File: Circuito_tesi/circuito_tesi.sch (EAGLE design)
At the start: 21 parts, among them IC1 317T, IC2 317T, IC3 317T, U1 NRF52832, U2 BME688, X1 OPAMP, X2 OPAMP

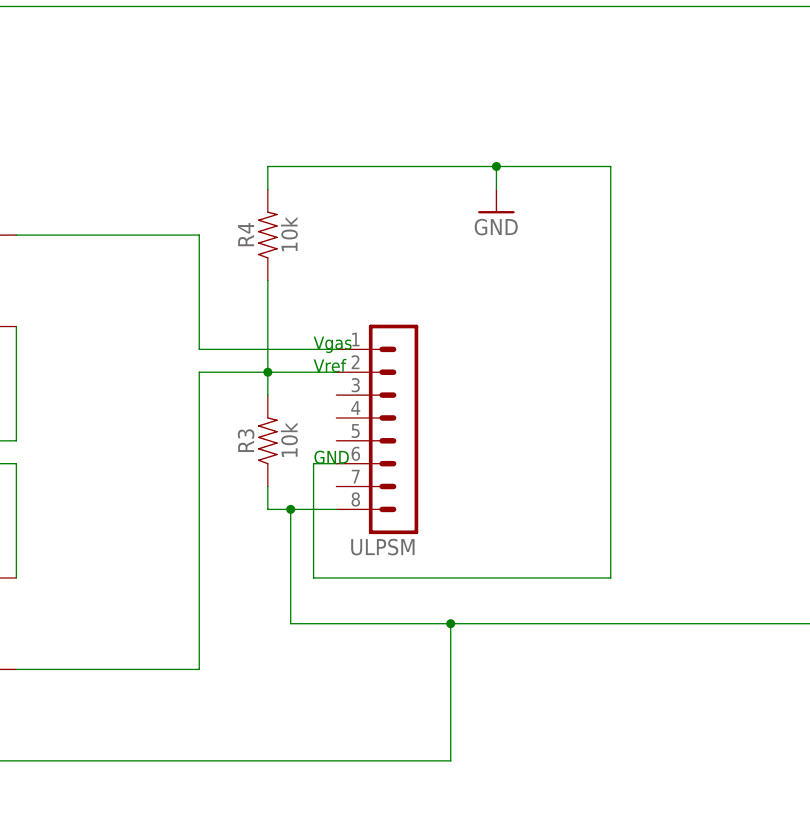
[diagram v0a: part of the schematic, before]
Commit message: Attivato saadc
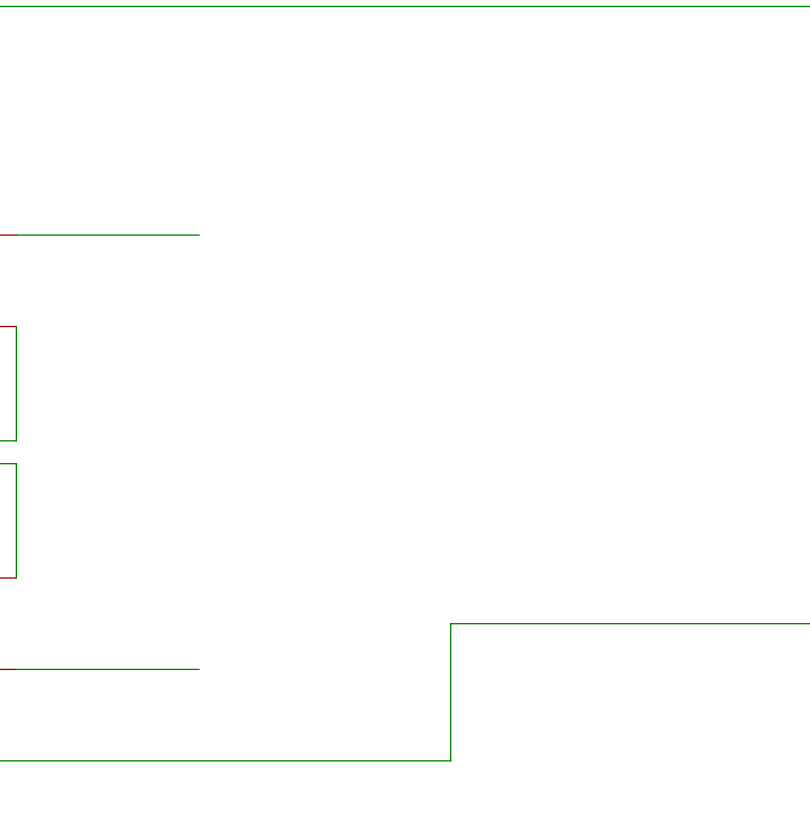
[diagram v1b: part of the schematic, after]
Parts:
- removed R3, R4: 10k, SparkFun-Resistors:10KOHM-HORIZ-1/6W-5%
- removed ULPSM: (no value), con-lstb:MA08-1
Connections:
- net 3.3: no longer R3.1, R4.2, ULPSM.6, ULPSM.8
- net N$10: no longer ULPSM.1
- net N$6: no longer R3.2, R4.1, ULPSM.2
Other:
- note removed: "GND"
- note removed: "Vgas"
- note removed: "Vref"
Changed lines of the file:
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@@
 <part name="R2" library="SparkFun-Resistors" deviceset="10KOHM" device="-HORIZ-1/6W-5%" value="10k"/>
 <part name="GND7" library="supply" deviceset="GND" device=""/>
-<part name="ULPSM" library="con-lstb" library_urn="urn:adsk.eagle:library:162" deviceset="MA08-1" device="" package3d_urn="urn:adsk.eagle:package:8343/1"/>
-<part name="R3" library="SparkFun-Resistors" deviceset="10KOHM" device="-HORIZ-1/6W-5%" value="10k"/>
-<part name="R4" library="SparkFun-Resistors" deviceset="10KOHM" device="-HORIZ-1/6W-5%" value="10k"/>
-<part name="GND8" library="supply" deviceset="GND" device=""/>
 <part name="X1" library="ngspice-simulation" library_urn="urn:adsk.eagle:library:527439" deviceset="OPAMP" device=""/>
 <part name="X2" library="ngspice-simulation" library_urn="urn:adsk.eagle:library:527439" deviceset="OPAMP" device=""/>
@@
 <text x="-132.08" y="104.14" size="1.4224" layer="91">SDA</text>
 <text x="-132.08" y="78.74" size="1.4224" layer="91">SCL</text>
-<text x="48.26" y="185.42" size="1.4224" layer="91">GND</text>
-<text x="48.26" y="198.12" size="1.4224" layer="91">Vgas</text>
-<text x="48.26" y="195.58" size="1.4224" layer="91">Vref</text>
 <text x="-220.98" y="86.36" size="5.08" layer="91">BME688</text>
 </plain>
@@
 <instance part="GND7" gate="1" x="-193.04" y="83.82" smashed="yes">
 <attribute name="VALUE" x="-195.58" y="81.28" size="1.778" layer="96"/>
-</instance>
-<instance part="ULPSM" gate="1" x="58.42" y="190.5" smashed="yes" rot="R180">
-<attribute name="VALUE" x="59.69" y="203.2" size="1.778" layer="96" rot="R180"/>
-<attribute name="NAME" x="59.69" y="177.038" size="1.778" layer="95" rot="R180"/>
-</instance>
-<instance part="R3" gate="G$1" x="43.18" y="187.96" smashed="yes" rot="R90">
-<attribute name="NAME" x="41.656" y="187.96" size="1.778" layer="95" font="vector" rot="R90" align="bottom-center"/>
-<attribute name="VALUE" x="44.704" y="187.96" size="1.778" layer="96" font="vector" rot="R90" align="top-center"/>
-</instance>
-<instance part="R4" gate="G$1" x="43.18" y="210.82" smashed="yes" rot="R90">
-<attribute name="NAME" x="41.656" y="210.82" size="1.778" layer="95" font="vector" rot="R90" align="bottom-center"/>
-<attribute name="VALUE" x="44.704" y="210.82" size="1.778" layer="96" font="vector" rot="R90" align="top-center"/>
-</instance>
-<instance part="GND8" gate="1" x="68.58" y="213.36" smashed="yes">
-<attribute name="VALUE" x="66.04" y="210.82" size="1.778" layer="96"/>
 </instance>
 <instance part="X1" gate="G$1" x="2.54" y="205.74" smashed="yes" rot="MR0">
@@
 </segment>
 <segment>
-<pinref part="R4" gate="G$1" pin="2"/>
-<wire x1="43.18" y1="215.9" x2="43.18" y2="218.44" width="0.1524" layer="91"/>
-<wire x1="43.18" y1="218.44" x2="68.58" y2="218.44" width="0.1524" layer="91"/>
-<pinref part="GND8" gate="1" pin="GND"/>
-<wire x1="68.58" y1="218.44" x2="68.58" y2="215.9" width="0.1524" layer="91"/>
-<pinref part="ULPSM" gate="1" pin="6"/>
-<wire x1="50.8" y1="185.42" x2="48.26" y2="185.42" width="0.1524" layer="91"/>
-<wire x1="48.26" y1="185.42" x2="48.26" y2="172.72" width="0.1524" layer="91"/>
-<wire x1="48.26" y1="172.72" x2="81.28" y2="172.72" width="0.1524" layer="91"/>
-<wire x1="81.28" y1="172.72" x2="81.28" y2="218.44" width="0.1524" layer="91"/>
-<wire x1="81.28" y1="218.44" x2="68.58" y2="218.44" width="0.1524" layer="91"/>
-<junction x="68.58" y="218.44"/>
-</segment>
-<segment>
 <pinref part="X1" gate="G$1" pin="VSS"/>
 <pinref part="GND9" gate="1" pin="GND"/>
@@
 <wire x1="-228.6" y1="104.14" x2="-228.6" y2="119.38" width="0.1524" layer="91"/>
 <wire x1="111.76" y1="71.12" x2="-228.6" y2="71.12" width="0.1524" layer="91"/>
-<pinref part="ULPSM" gate="1" pin="8"/>
-<wire x1="50.8" y1="180.34" x2="45.72" y2="180.34" width="0.1524" layer="91"/>
-<wire x1="45.72" y1="180.34" x2="45.72" y2="167.64" width="0.1524" layer="91"/>
-<wire x1="45.72" y1="167.64" x2="63.5" y2="167.64" width="0.1524" layer="91"/>
 <junction x="111.76" y="167.64"/>
 <wire x1="63.5" y1="167.64" x2="111.76" y2="167.64" width="0.1524" layer="91"/>
-<wire x1="45.72" y1="180.34" x2="43.18" y2="180.34" width="0.1524" layer="91"/>
-<junction x="45.72" y="180.34"/>
-<pinref part="R3" gate="G$1" pin="1"/>
-<wire x1="43.18" y1="180.34" x2="43.18" y2="182.88" width="0.1524" layer="91"/>
 <pinref part="B1" gate="G$1" pin="LV"/>
 <pinref part="IC2" gate="A1" pin="VO"/>
@@
 <wire x1="0" y1="152.4" x2="63.5" y2="152.4" width="0.1524" layer="91"/>
 <wire x1="63.5" y1="152.4" x2="63.5" y2="167.64" width="0.1524" layer="91"/>
-<junction x="63.5" y="167.64"/>
 <wire x1="-228.6" y1="119.38" x2="-190.5" y2="119.38" width="0.1524" layer="91"/>
 <pinref part="U2" gate="G$1" pin="VDDIO"/>
@@
 <net name="N$6" class="0">
 <segment>
-<pinref part="R3" gate="G$1" pin="2"/>
-<wire x1="43.18" y1="193.04" x2="43.18" y2="195.58" width="0.1524" layer="91"/>
-<pinref part="ULPSM" gate="1" pin="2"/>
-<wire x1="43.18" y1="195.58" x2="50.8" y2="195.58" width="0.1524" layer="91"/>
-<pinref part="R4" gate="G$1" pin="1"/>
-<wire x1="43.18" y1="195.58" x2="43.18" y2="205.74" width="0.1524" layer="91"/>
-<junction x="43.18" y="195.58"/>
-<wire x1="35.56" y1="162.56" x2="35.56" y2="195.58" width="0.1524" layer="91"/>
-<wire x1="35.56" y1="195.58" x2="43.18" y2="195.58" width="0.1524" layer="91"/>
 <pinref part="X2" gate="G$1" pin="P"/>
 <wire x1="15.24" y1="162.56" x2="35.56" y2="162.56" width="0.1524" layer="91"/>
@@
 <pinref part="X1" gate="G$1" pin="P"/>
 <wire x1="15.24" y1="210.82" x2="35.56" y2="210.82" width="0.1524" layer="91"/>
-<wire x1="35.56" y1="210.82" x2="35.56" y2="198.12" width="0.1524" layer="91"/>
-<pinref part="ULPSM" gate="1" pin="1"/>
-<wire x1="35.56" y1="198.12" x2="50.8" y2="198.12" width="0.1524" layer="91"/>
-</segment>
-</net>
+</segment>
+</net>

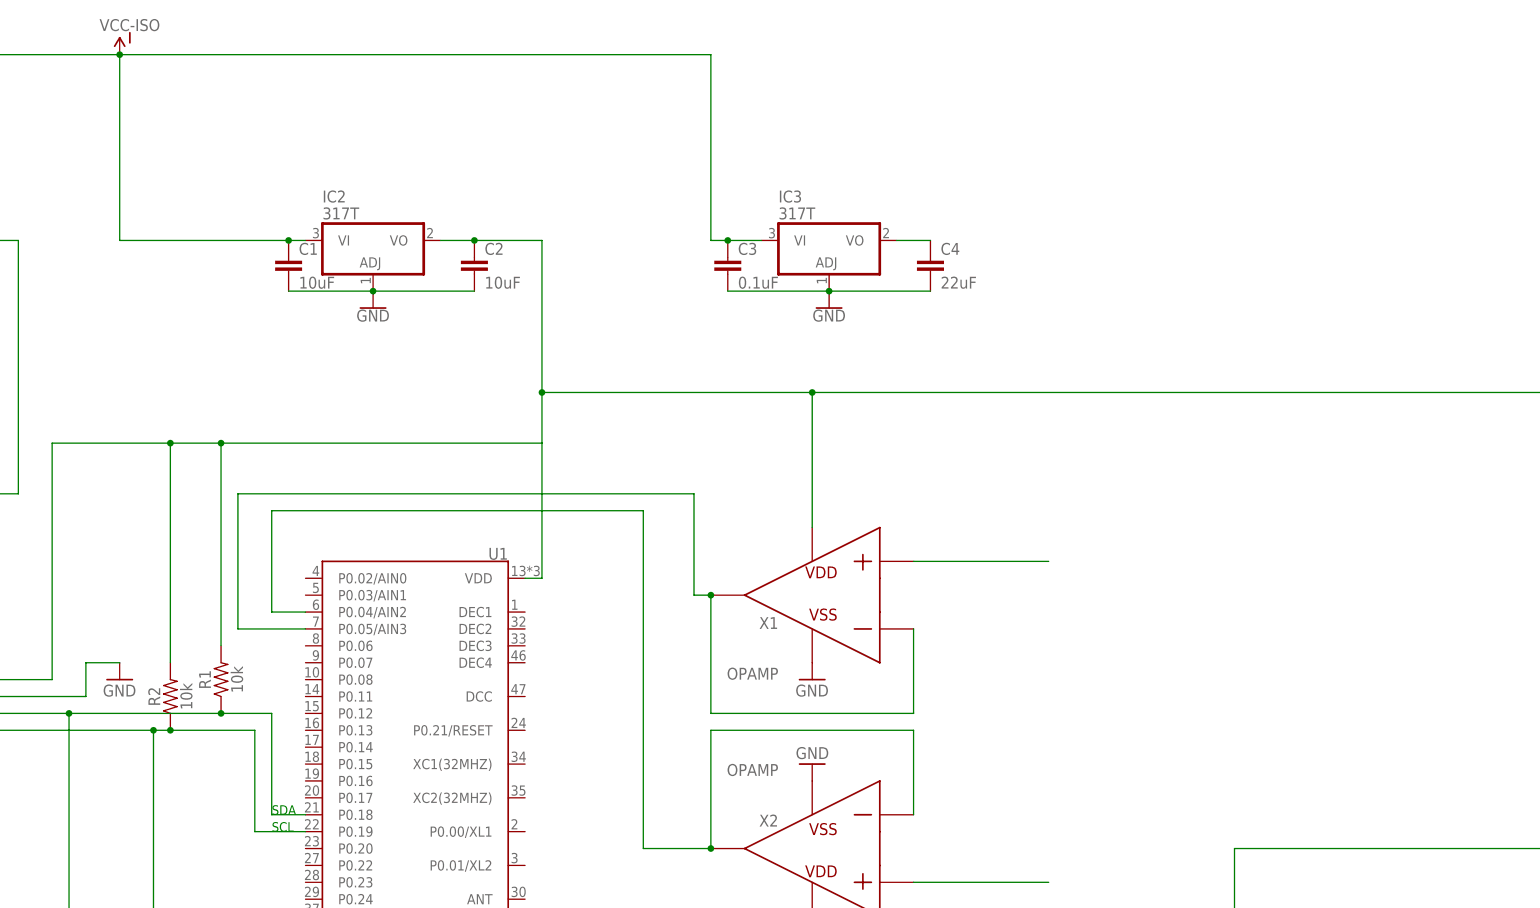
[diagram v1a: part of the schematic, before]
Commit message: Aggiunta lettura MICS6814
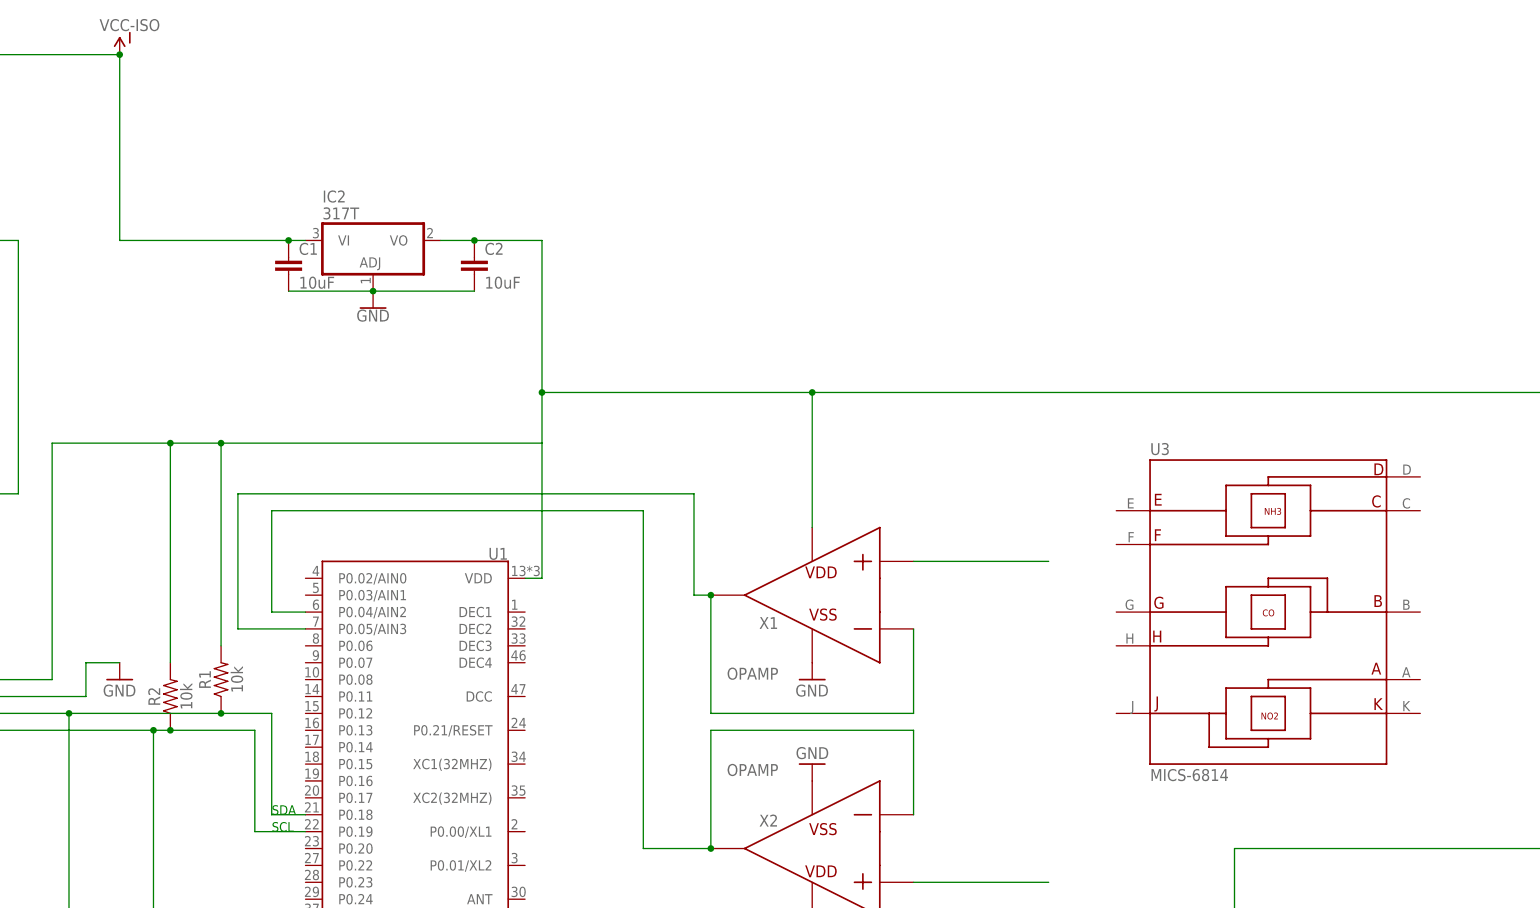
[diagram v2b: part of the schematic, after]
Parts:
- removed C3: 0.1uF, SparkFun-Capacitors:0.1UF-0603-25V-5%
- removed C4: 22uF, SparkFun-Capacitors:22UF-0805-6.3V-20%
- removed IC3: 317T, linear:317T
- added U3: MICS-6814, MICS-6814:MICS-6814
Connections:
- removed net N$2: C4.1, IC3.VO
- net 3.3: no longer C3.2, C4.2, IC3.ADJ
- net VCC-ISO: no longer C3.1, IC3.VI
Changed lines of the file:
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@@
 <part name="IC1" library="linear" library_urn="urn:adsk.eagle:library:262" deviceset="*317" device="T" package3d_urn="urn:adsk.eagle:package:16414/1"/>
 <part name="IC2" library="linear" library_urn="urn:adsk.eagle:library:262" deviceset="*317" device="T" package3d_urn="urn:adsk.eagle:package:16414/1"/>
-<part name="IC3" library="linear" library_urn="urn:adsk.eagle:library:262" deviceset="*317" device="T" package3d_urn="urn:adsk.eagle:package:16414/1"/>
 <part name="GND1" library="SparkFun-PowerSymbols" deviceset="GND" device=""/>
-<part name="GND2" library="SparkFun-PowerSymbols" deviceset="GND" device=""/>
 <part name="GND3" library="SparkFun-PowerSymbols" deviceset="GND" device=""/>
 <part name="B1" library="SparkFun-Boards" deviceset="SPARKFUN_LOGIC_LEVEL_CONVERTER" device=""/>
 <part name="C1" library="SparkFun-Capacitors" deviceset="10UF" device="-0805-10V-10%" value="10uF"/>
 <part name="C2" library="SparkFun-Capacitors" deviceset="10UF" device="-0805-10V-10%" value="10uF"/>
-<part name="C3" library="SparkFun-Capacitors" deviceset="0.1UF" device="-0603-25V-5%" value="0.1uF"/>
-<part name="C4" library="SparkFun-Capacitors" deviceset="22UF" device="-0805-6.3V-20%" value="22uF"/>
 <part name="C5" library="SparkFun-Capacitors" deviceset="0.33UF/330NF" device="-0805-50V-10%" value="0.33µF"/>
 <part name="C6" library="SparkFun-Capacitors" deviceset="0.1UF" device="-0603-25V-5%" value="0.1uF"/>
@@
 <part name="SCD4X" library="SCD41-D-R1" deviceset="SCD4X" device="SCD4X_SCD4X_SCD4X"/>
 <part name="GND11" library="supply" deviceset="GND" device=""/>
+<part name="U3" library="MICS-6814" deviceset="MICS-6814" device=""/>
 </parts>
 <sheets>
@@
 <attribute name="VALUE" x="-73.66" y="262.255" size="1.778" layer="96"/>
 </instance>
-<instance part="IC3" gate="A1" x="2.54" y="256.54" smashed="yes">
-<attribute name="NAME" x="-5.08" y="264.795" size="1.778" layer="95"/>
-<attribute name="VALUE" x="-5.08" y="262.255" size="1.778" layer="96"/>
-</instance>
 <instance part="GND1" gate="1" x="-66.04" y="248.92" smashed="yes">
 <attribute name="VALUE" x="-66.04" y="248.666" size="1.778" layer="96" align="top-center"/>
-</instance>
-<instance part="GND2" gate="1" x="2.54" y="248.92" smashed="yes">
-<attribute name="VALUE" x="2.54" y="248.666" size="1.778" layer="96" align="top-center"/>
 </instance>
 <instance part="GND3" gate="1" x="-147.32" y="248.92" smashed="yes">
@@
 <attribute name="VALUE" x="-49.276" y="251.841" size="1.778" layer="96" font="vector"/>
 </instance>
-<instance part="C3" gate="G$1" x="-12.7" y="254" smashed="yes">
-<attribute name="NAME" x="-11.176" y="256.921" size="1.778" layer="95" font="vector"/>
-<attribute name="VALUE" x="-11.176" y="251.841" size="1.778" layer="96" font="vector"/>
-</instance>
-<instance part="C4" gate="G$1" x="17.78" y="254" smashed="yes">
-<attribute name="NAME" x="19.304" y="256.921" size="1.778" layer="95" font="vector"/>
-<attribute name="VALUE" x="19.304" y="251.841" size="1.778" layer="96" font="vector"/>
-</instance>
 <instance part="C5" gate="G$1" x="-162.56" y="254" smashed="yes">
 <attribute name="NAME" x="-161.036" y="256.921" size="1.778" layer="95" font="vector"/>
@@
 <instance part="GND11" gate="1" x="-223.52" y="129.54" smashed="yes">
 <attribute name="VALUE" x="-226.06" y="127" size="1.778" layer="96"/>
+</instance>
+<instance part="U3" gate="G$1" x="68.58" y="203.2" smashed="yes">
+<attribute name="NAME" x="50.8" y="226.822" size="1.778" layer="95"/>
+<attribute name="VALUE" x="50.8" y="177.8" size="1.778" layer="96"/>
 </instance>
 </instances>
@@
 <wire x1="-162.56" y1="259.08" x2="-157.48" y2="259.08" width="0.1524" layer="91"/>
 <junction x="-162.56" y="259.08"/>
-<wire x1="-104.14" y1="287.02" x2="-15.24" y2="287.02" width="0.1524" layer="91"/>
-<wire x1="-15.24" y1="287.02" x2="-15.24" y2="259.08" width="0.1524" layer="91"/>
-<pinref part="IC3" gate="A1" pin="VI"/>
-<wire x1="-15.24" y1="259.08" x2="-12.7" y2="259.08" width="0.1524" layer="91"/>
-<pinref part="C3" gate="G$1" pin="1"/>
-<wire x1="-12.7" y1="259.08" x2="-7.62" y2="259.08" width="0.1524" layer="91"/>
-<junction x="-12.7" y="259.08"/>
 </segment>
 </net>
@@
 <pinref part="C2" gate="G$1" pin="2"/>
 <wire x1="-50.8" y1="251.46" x2="-66.04" y2="251.46" width="0.1524" layer="91"/>
-</segment>
-<segment>
-<pinref part="IC3" gate="A1" pin="ADJ"/>
-<pinref part="GND2" gate="1" pin="GND"/>
-<pinref part="C4" gate="G$1" pin="2"/>
-<wire x1="17.78" y1="251.46" x2="2.54" y2="251.46" width="0.1524" layer="91"/>
-<junction x="2.54" y="251.46"/>
-<pinref part="C3" gate="G$1" pin="2"/>
-<wire x1="-12.7" y1="251.46" x2="2.54" y2="251.46" width="0.1524" layer="91"/>
 </segment>
 <segment>
@@
 </segment>
 </net>
-<net name="N$2" class="0">
-<segment>
-<pinref part="IC3" gate="A1" pin="VO"/>
-<pinref part="C4" gate="G$1" pin="1"/>
-<wire x1="12.7" y1="259.08" x2="17.78" y2="259.08" width="0.1524" layer="91"/>
-</segment>
-</net>

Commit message: Completato schematico (resistenze non corrette)
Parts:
- added 10_MOHM, 10_MOHM1, 10_MOHM2, 130OHM, 27OHM, 5_MOHM, 5_MOHM1, 5_MOHM2, 820OHM: 1614992-1, 1614992-1:1614992-1
- added BT1, BT2, BT3, BT4: BHX1-2450-SM, BHX1-2450-SM:BHX1-2450-SM
- added C3, C4, C7: (no value), capacitor-wima:C2,5-3
- added X3: OPAMP, ngspice-simulation:OPAMP
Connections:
- removed net VCC-ISO: C1.1, C5.1, IC1.VI, IC2.VI
- new net N$11: 820OHM.1, U3.RH2_NH3, U3.RH2_RED
- new net N$12: 27OHM.1, U3.RH1_NH3
- new net N$13: 130OHM.1, U3.RH2_OX
- new net N$14: U3.RS1_NH3, X3.P
- new net N$15: 5_MOHM.2, X1.N, X1.VOUT
- new net N$16: 10_MOHM2.2, 5_MOHM2.1, C3.1, U1.P0.04/AIN2
- new net N$17: 10_MOHM.2, 5_MOHM.1, C7.1, U1.P0.05/AIN3
- new net N$18: 10_MOHM1.2, 5_MOHM1.1, C4.1, U1.P0.03/AIN1
- new net N$2: BT1.-, BT2.+
- new net N$4: BT2.-, BT3.+
- new net N$5: BT3.-, BT4.+
- new net N$9: BT1.+, C1.1, C5.1, IC1.VI, IC2.VI
- net 3.3: no longer X1.VDD, X2.VDD
- net 5V: now also 130OHM.2, 27OHM.2, 820OHM.2, X1.VDD, X2.VDD, X3.VDD
- net GND: now also 10_MOHM.1, 10_MOHM1.1, 10_MOHM2.1, BT4.-, C3.2, C4.2, C7.2, U3.RH1/RS1_OX, U3.RH1/RS1_RED, U3.RS2_NH3, X3.VSS
- net N$10: now also U3.RS2_RED
- net N$6: now also U3.RS2
- net N$7: now also 5_MOHM1.2; no longer U1.P0.04/AIN2
- net N$8: now also 5_MOHM2.2, X3.N, X3.VOUT; no longer U1.P0.05/AIN3, X1.N, X1.VOUT
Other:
- note added: "ATTENZIONE: resistenze mics non corrispondono ai valori richiesti, valore scritto in numero"
- moved on the sheet: U3, X1, X2

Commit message: modifica board
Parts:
- removed X1, X2, X3: OPAMP, ngspice-simulation:OPAMP
- added 300_OHM: 1614992-1, 1614992-1:1614992-1
- added LED1: LAP4-BOTTOM, led:LAP4-BOTTOM
- added S1: GF-123-0054, GF-123-0054:GF-123-0054
- added U4, U5: OPA2277PA, OPA2277PA:OPA2277PA
- renumbered IC1 to IC5, IC2 to IC3.3
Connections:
- removed net N$15: 5_MOHM.2, X1.N, X1.VOUT
- new net N$19: BT1.+, S1.1
- new net N$21: LED1.A, U1.P0.23
- new net N$22: 5_MOHM.2, U4.-IN_A, U4.OUT_A
- new net VDD: C1.1, C5.1, IC3.3.VI, IC5.VI, S1.2
- net 3.3: no longer C1.2, C2.2, C5.2, C6.2, IC3.3.ADJ, IC5.ADJ, X1.VSS, X2.VSS
- net 5V: now also U4.V+, U5.V+; no longer X1.VDD, X2.VDD, X3.VDD
- net GND: now also 300_OHM.1, C1.2, C2.2, C5.2, C6.2, IC3.3.ADJ, IC5.ADJ, U4.V-, U5.V-; no longer X3.VSS
- net N$10: now also U4.+IN_A; no longer X1.P
- net N$14: now also U5.+IN_A; no longer X3.P
- net N$6: now also U4.+IN_B; no longer X2.P
- net N$7: now also U4.-IN_B, U4.OUT_B; no longer X2.N, X2.VOUT
- net N$8: now also U5.-IN_A, U5.OUT_A; no longer X3.N, X3.VOUT
- net N$9: now also 300_OHM.2, LED1.C; no longer BT1.+, C1.1, C5.1, IC3.3.VI, IC5.VI
